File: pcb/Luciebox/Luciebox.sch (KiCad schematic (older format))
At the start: 56 parts, among them J1 Screw_Terminal_01x07, J2 Screw_Terminal_01x07, J3 Screw_Terminal_01x07, J4 Screw_Terminal_01x07, J5 Screw_Terminal_01x07, P1 CONN_01X01, P2 CONN_01X01, P3 CONN_01X01, P4 CONN_01X01, P5 Digital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

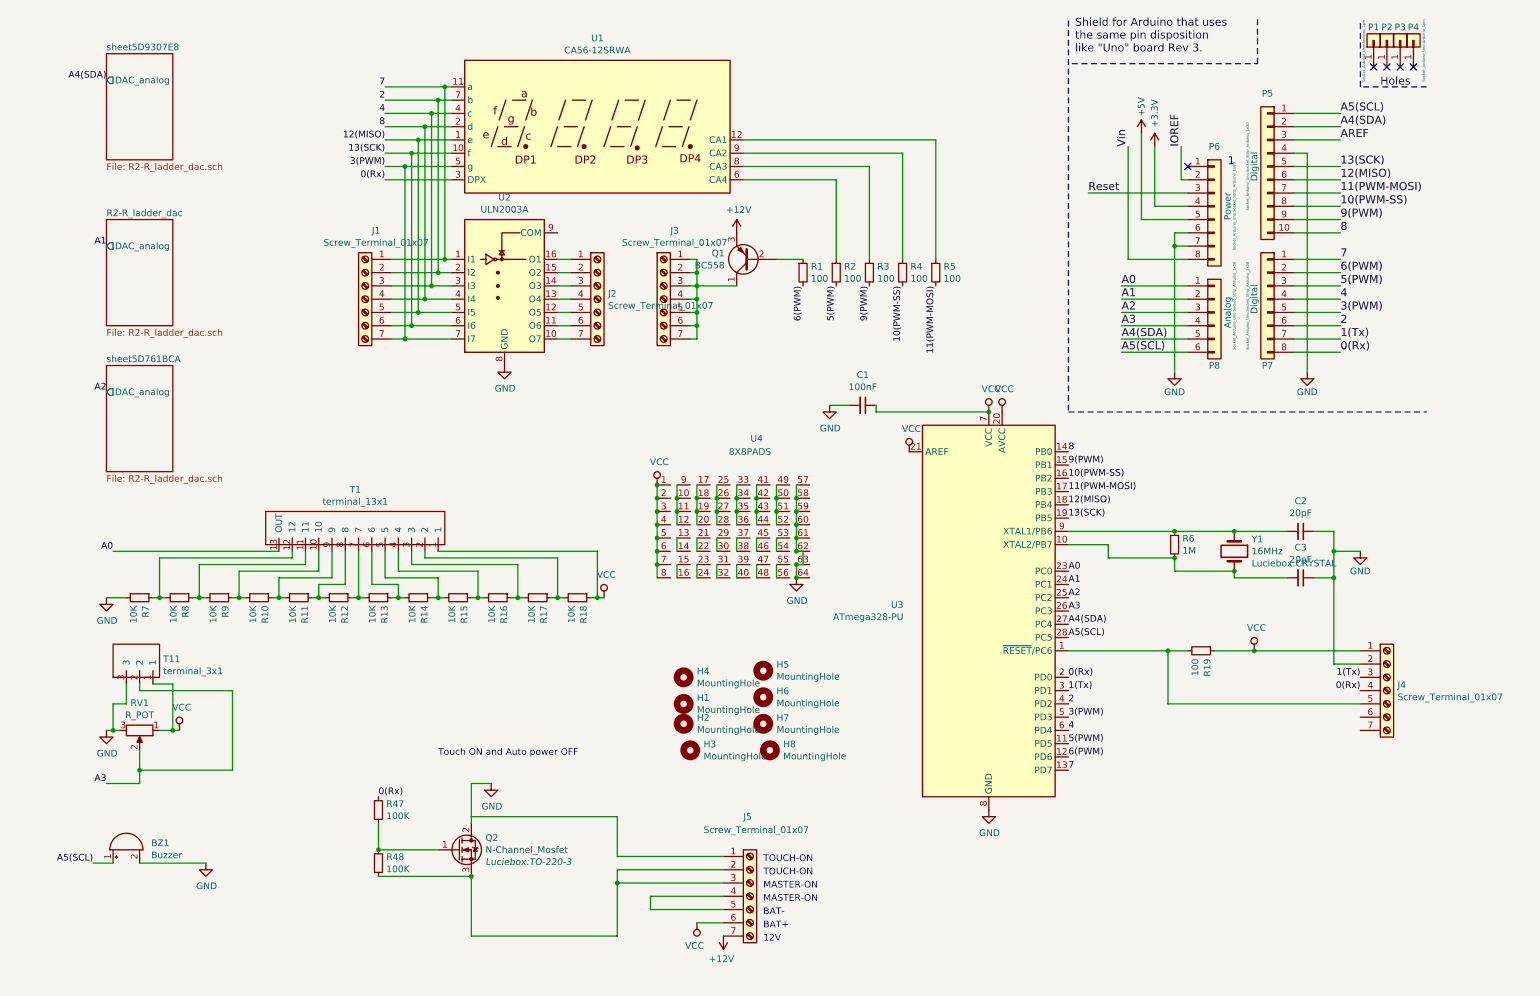
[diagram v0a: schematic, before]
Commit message: buttons and selector switch debugging. Starting to change pcb schematic for v2.0 board
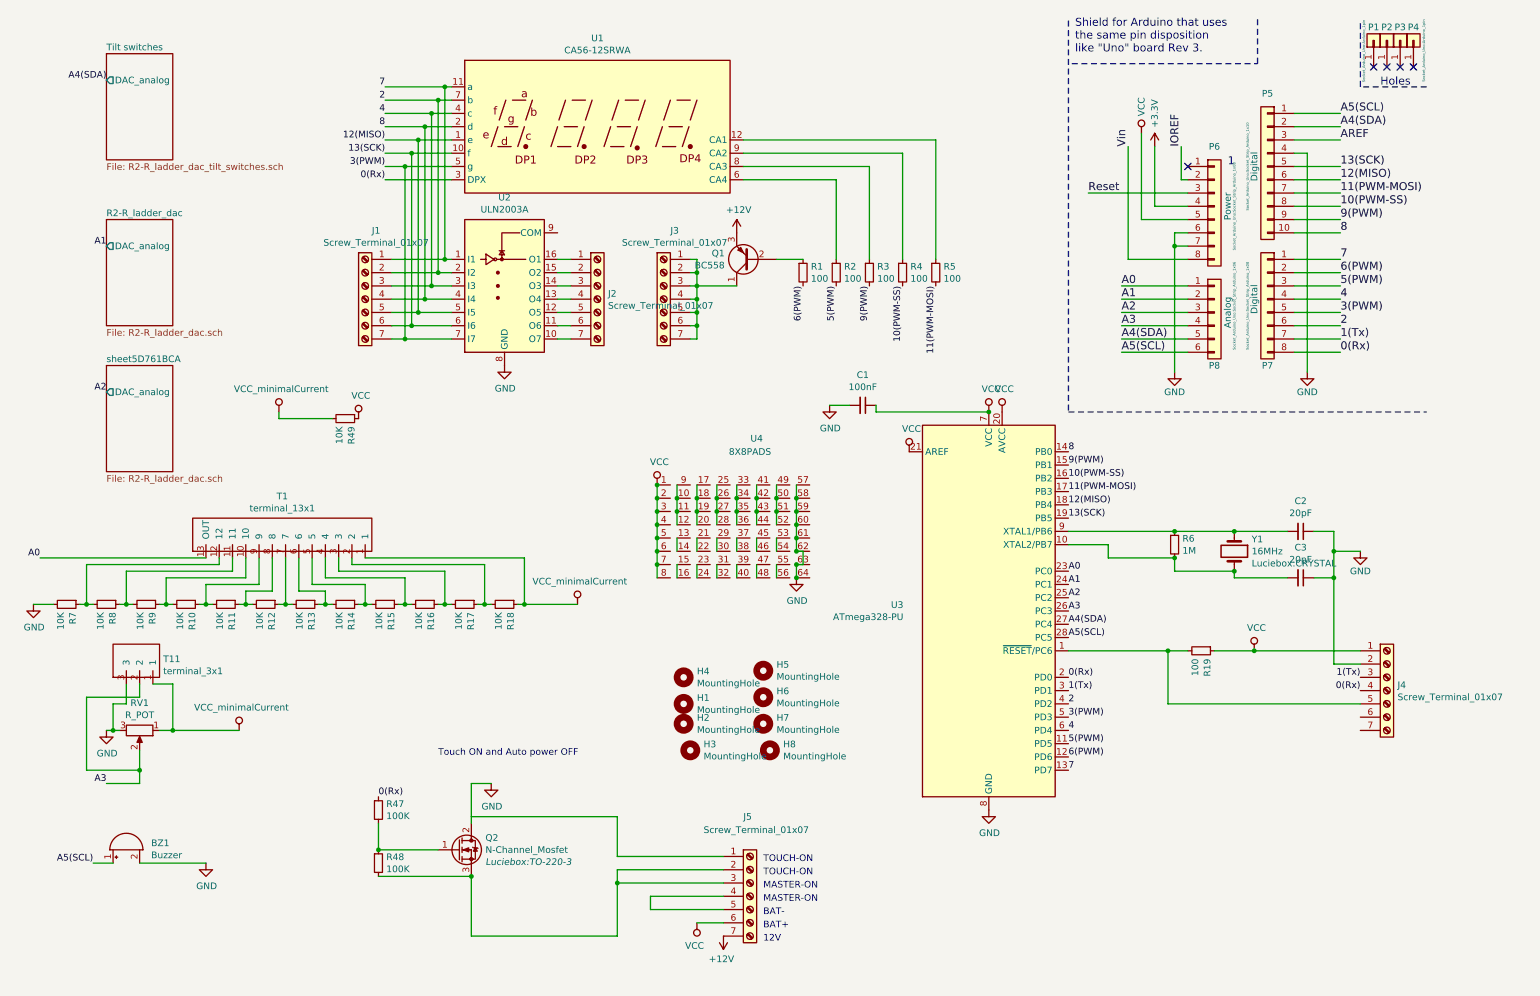
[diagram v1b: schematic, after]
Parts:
- added R49: 10K, Luciebox:1206, symbol Device:R_Small
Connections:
- net +5V is gone; now on net VCC: P6.5 (Pin_5)
- net VCC: now also R49.1; no longer R18.1, RV1.1, T1.1, T11.1
- new net VCC_minimalCurrent: R18.1, R49.2, RV1.1, T1.1, T11.1
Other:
- moved on the sheet: R10, R11, R12, R13, R14, R15, R16, R17, R18, R7, R8, R9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

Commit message: changes in pcb v2.0
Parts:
- added D1: D_Schottky, Luciebox:smd_throughhole_2_pins, symbol Luciebox_components:D_Schottky
- added J7: USB_B_Mini, Luciebox:usb_mini_Molex-0548190519, symbol Connector:USB_B_Mini
- added T8: terminal_3x1, Luciebox:Terminal_3x1_100mil, symbol Luciebox_components:terminal_3x1
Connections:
- net GND: now also J7.5 (GND), J7.6 (Shield)
- net VCC: now also D1.1 (K)
- new net: D1.2 (A), J7.1 (VBUS)
- new net: J7.2 (D-), T8.2
- new net: J7.3 (D+), T8.3
- new net: J7.4 (ID), T8.1
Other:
- moved on the sheet: J5, Q2, R47, R48
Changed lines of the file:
@@
 EESchema Schematic File Version 4
 LIBS:Luciebox-cache
-EELAYER 30 0
+EELAYER 29 0
 EELAYER END
 $Descr A4 11693 8268
@@
 L Luciebox_components:N-Channel_Mosfet Q2
 U 1 1 5D6BDEDC
-P 3900 6750
-F 0 "Q2" H 4106 6841 50  0000 L CNN
-F 1 "N-Channel_Mosfet" H 4106 6750 50  0000 L CNN
-F 2 "Luciebox:TO-220-3" H 4106 6659 50  0000 L CIN
-F 3 "https://www.onsemi.com/pub/Collateral/FQP30N06L-D.pdf" V 3900 6750 50  0001 L CNN
-	1    3900 6750
+P 3950 6900
+F 0 "Q2" H 4156 6991 50  0000 L CNN
+F 1 "N-Channel_Mosfet" H 4156 6900 50  0000 L CNN
+F 2 "Luciebox:TO-220-3" H 4156 6809 50  0000 L CIN
+F 3 "https://www.onsemi.com/pub/Collateral/FQP30N06L-D.pdf" V 3950 6900 50  0001 L CNN
+	1    3950 6900
 	1    0    0    -1
 $EndComp
@@
 L Device:R_Small R47
 U 1 1 5D6C3437
-P 3300 6450
-F 0 "R47" H 3359 6496 50  0000 L CNN
-F 1 "100K" H 3359 6405 50  0000 L CNN
-F 2 "Luciebox:1206" H 3300 6450 50  0001 C CNN
-F 3 "~" H 3300 6450 50  0001 C CNN
-	1    3300 6450
+P 3350 6600
+F 0 "R47" H 3409 6646 50  0000 L CNN
+F 1 "100K" H 3409 6555 50  0000 L CNN
+F 2 "Luciebox:1206" H 3350 6600 50  0001 C CNN
+F 3 "~" H 3350 6600 50  0001 C CNN
+	1    3350 6600
 	1    0    0    -1
 $EndComp
@@
 L Device:R_Small R48
 U 1 1 5D6C3ACD
-P 3300 6850
-F 0 "R48" H 3359 6896 50  0000 L CNN
-F 1 "100K" H 3359 6805 50  0000 L CNN
-F 2 "Luciebox:1206" H 3300 6850 50  0001 C CNN
-F 3 "~" H 3300 6850 50  0001 C CNN
-	1    3300 6850
-	1    0    0    -1
-$EndComp
-Wire Wire Line
-	3300 6550 3300 6750
-Connection ~ 3300 6750
-Text Label 3300 6350 0    50   ~ 0
+P 3350 7000
+F 0 "R48" H 3409 7046 50  0000 L CNN
+F 1 "100K" H 3409 6955 50  0000 L CNN
+F 2 "Luciebox:1206" H 3350 7000 50  0001 C CNN
+F 3 "~" H 3350 7000 50  0001 C CNN
+	1    3350 7000
+	1    0    0    -1
+$EndComp
+Wire Wire Line
+	3350 6700 3350 6900
+Connection ~ 3350 6900
+Text Label 3350 6500 0    50   ~ 0
 0(Rx)
 $Comp
 L power:GND #PWR0101
 U 1 1 5D70EC69
-P 4150 6250
-F 0 "#PWR0101" H 4150 6000 50  0001 C CNN
-F 1 "GND" H 4155 6077 50  0000 C CNN
-F 2 "" H 4150 6250 50  0001 C CNN
-F 3 "" H 4150 6250 50  0001 C CNN
-	1    4150 6250
-	1    0    0    -1
-$EndComp
-Wire Wire Line
-	4000 6950 3300 6950
-Wire Wire Line
-	4150 6250 4000 6250
-Wire Wire Line
-	4000 6250 4000 6500
-Wire Wire Line
-	4000 6950 4000 7400
-Connection ~ 4000 6950
+P 4200 6400
+F 0 "#PWR0101" H 4200 6150 50  0001 C CNN
+F 1 "GND" H 4205 6227 50  0000 C CNN
+F 2 "" H 4200 6400 50  0001 C CNN
+F 3 "" H 4200 6400 50  0001 C CNN
+	1    4200 6400
+	1    0    0    -1
+$EndComp
+Wire Wire Line
+	4050 7100 3350 7100
+Wire Wire Line
+	4200 6400 4050 6400
+Wire Wire Line
+	4050 6400 4050 6650
+Wire Wire Line
+	4050 7100 4050 7550
+Connection ~ 4050 7100
 $Comp
 L Connector:Screw_Terminal_01x07 J5
 U 1 1 5D74D272
-P 6100 7100
-F 0 "J5" H 6050 7700 50  0000 L CNN
-F 1 "Screw_Terminal_01x07" H 5750 7600 50  0000 L CNN
-F 2 "Luciebox:Terminal_7x1_100mil" H 6100 7100 50  0001 C CNN
-F 3 "~" H 6100 7100 50  0001 C CNN
-	1    6100 7100
-	1    0    0    -1
-$EndComp
-Wire Wire Line
-	5100 6500 4000 6500
-Wire Wire Line
-	4000 6500 4000 6550
-Wire Wire Line
-	5900 6800 5100 6800
-Wire Wire Line
-	5100 6800 5100 6500
-Wire Wire Line
-	5900 6900 5100 6900
-Wire Wire Line
-	5100 7400 4000 7400
-Wire Wire Line
-	5100 6900 5100 7000
-Wire Wire Line
-	5900 7000 5100 7000
-Connection ~ 5100 7000
-Wire Wire Line
-	5100 7000 5100 7400
-Wire Wire Line
-	5900 7100 5350 7100
+P 6150 7250
+F 0 "J5" H 6100 7850 50  0000 L CNN
+F 1 "Screw_Terminal_01x07" H 5800 7750 50  0000 L CNN
+F 2 "Luciebox:Terminal_7x1_100mil" H 6150 7250 50  0001 C CNN
+F 3 "~" H 6150 7250 50  0001 C CNN
+	1    6150 7250
+	1    0    0    -1
+$EndComp
+Wire Wire Line
+	5150 6650 4050 6650
+Wire Wire Line
+	4050 6650 4050 6700
+Wire Wire Line
+	5950 6950 5150 6950
+Wire Wire Line
+	5150 6950 5150 6650
+Wire Wire Line
+	5950 7050 5150 7050
+Wire Wire Line
+	5150 7550 4050 7550
+Wire Wire Line
+	5150 7050 5150 7150
+Wire Wire Line
+	5950 7150 5150 7150
+Connection ~ 5150 7150
+Wire Wire Line
+	5150 7150 5150 7550
+Wire Wire Line
+	5950 7250 5400 7250
 $Comp
 L power:VCC #PWR0102
 U 1 1 5D7FF3DB
-P 5700 7300
-F 0 "#PWR0102" H 5700 7150 50  0001 C CNN
-F 1 "VCC" H 5718 7473 50  0000 C CNN
-F 2 "" H 5700 7300 50  0001 C CNN
-F 3 "" H 5700 7300 50  0001 C CNN
-	1    5700 7300
+P 5750 7450
+F 0 "#PWR0102" H 5750 7300 50  0001 C CNN
+F 1 "VCC" H 5768 7623 50  0000 C CNN
+F 2 "" H 5750 7450 50  0001 C CNN
+F 3 "" H 5750 7450 50  0001 C CNN
+	1    5750 7450
 	-1   0    0    1
 $EndComp
-Text Notes 6200 7350 0    50   ~ 0
+Text Notes 6250 7500 0    50   ~ 0
 BAT+
-Text Notes 6200 7250 0    50   ~ 0
+Text Notes 6250 7400 0    50   ~ 0
 BAT-
-Text Notes 6200 7050 0    50   ~ 0
+Text Notes 6250 7200 0    50   ~ 0
 MASTER-ON
-Text Notes 6200 7150 0    50   ~ 0
+Text Notes 6250 7300 0    50   ~ 0
 MASTER-ON
-Text Notes 6200 6850 0    50   ~ 0
+Text Notes 6250 7000 0    50   ~ 0
 TOUCH-ON
-Text Notes 6200 6950 0    50   ~ 0
+Text Notes 6250 7100 0    50   ~ 0
 TOUCH-ON
 Wire Wire Line
-	5350 7200 5350 7100
-Wire Wire Line
-	5350 7200 5900 7200
-Wire Wire Line
-	5900 7300 5700 7300
-Text Notes 3750 6050 0    50   ~ 0
+	5400 7350 5400 7250
+Wire Wire Line
+	5400 7350 5950 7350
+Wire Wire Line
+	5950 7450 5750 7450
+Text Notes 3300 6350 0    50   ~ 0
 Touch ON and Auto power OFF
 $Comp
@@
 	1500 6150 1100 6150
 Wire Wire Line
-	3300 6750 3750 6750
+	3350 6900 3800 6900
 $Comp
 L power:+12V #PWR0103
 U 1 1 5DC88B13
-P 5900 7400
-F 0 "#PWR0103" H 5900 7250 50  0001 C CNN
-F 1 "+12V" H 5915 7573 50  0000 C CNN
-F 2 "" H 5900 7400 50  0001 C CNN
-F 3 "" H 5900 7400 50  0001 C CNN
-	1    5900 7400
+P 5950 7550
+F 0 "#PWR0103" H 5950 7400 50  0001 C CNN
+F 1 "+12V" H 5965 7723 50  0000 C CNN
+F 2 "" H 5950 7550 50  0001 C CNN
+F 3 "" H 5950 7550 50  0001 C CNN
+	1    5950 7550
 	-1   0    0    1
 $EndComp
-Text Notes 6200 7450 0    50   ~ 0
+Text Notes 6250 7600 0    50   ~ 0
 12V
 $Comp
@@
 Wire Wire Line
 	1750 5850 2250 5850
+$Comp
+L Connector:USB_B_Mini J7
+U 1 1 5E641E20
+P 4700 5800
+F 0 "J7" H 4470 5697 50  0000 R CNN
+F 1 "USB_B_Mini" H 4470 5788 50  0000 R CNN
+F 2 "Luciebox:usb_mini_Molex-0548190519" H 4850 5750 50  0001 C CNN
+F 3 "~" H 4850 5750 50  0001 C CNN
+	1    4700 5800
+	-1   0    0    1
+$EndComp
+$Comp
+L Luciebox_components:D_Schottky D1
+U 1 1 5E65D2EA
+P 4050 6000
+F 0 "D1" H 4050 6216 50  0000 C CNN
+F 1 "D_Schottky" H 4050 6125 50  0000 C CNN
+F 2 "Luciebox:smd_throughhole_2_pins" H 4050 6000 50  0001 C CNN
+F 3 "~" H 4050 6000 50  0001 C CNN
+	1    4050 6000
+	1    0    0    -1
+$EndComp
+Connection ~ 4050 6650
+Wire Wire Line
+	4400 6000 4200 6000
+$Comp
+L power:VCC #PWR0104
+U 1 1 5E6FDF29
+P 3700 6000
+F 0 "#PWR0104" H 3700 5850 50  0001 C CNN
+F 1 "VCC" H 3717 6173 50  0000 C CNN
+F 2 "" H 3700 6000 50  0001 C CNN
+F 3 "" H 3700 6000 50  0001 C CNN
+	1    3700 6000
+	1    0    0    -1
+$EndComp
+Wire Wire Line
+	3700 6000 3900 6000
+$Comp
+L power:GND #PWR0105
+U 1 1 5E716C2D
+P 5150 5350
+F 0 "#PWR0105" H 5150 5100 50  0001 C CNN
+F 1 "GND" H 5155 5177 50  0000 C CNN
+F 2 "" H 5150 5350 50  0001 C CNN
+F 3 "" H 5150 5350 50  0001 C CNN
+	1    5150 5350
+	1    0    0    -1
+$EndComp
+Wire Wire Line
+	5150 5350 4800 5350
+Wire Wire Line
+	4800 5350 4800 5400
+Wire Wire Line
+	4800 5350 4700 5350
+Wire Wire Line
+	4700 5350 4700 5400
+Connection ~ 4800 5350
+$Comp
+L Luciebox_components:terminal_3x1 T8
+U 1 1 5E74AAC5
+P 4000 5400
+F 0 "T8" H 4092 5185 50  0000 C CNN
+F 1 "terminal_3x1" H 4092 5276 50  0000 C CNN
+F 2 "Luciebox:Terminal_3x1_100mil" H 3800 5300 50  0001 C CNN
+F 3 "" H 3950 5800 50  0001 C CNN
+	1    4000 5400
+	-1   0    0    1
+$EndComp
+Wire Wire Line
+	4050 5400 4400 5400
+Wire Wire Line
+	4400 5400 4400 5600
+Wire Wire Line
+	4050 5500 4350 5500
+Wire Wire Line
+	4350 5500 4350 5700
+Wire Wire Line
+	4350 5700 4400 5700
+Wire Wire Line
+	4400 5800 4150 5800
+Wire Wire Line
+	4150 5800 4150 5600
+Wire Wire Line
+	4150 5600 4050 5600
 $EndSCHEMATC
